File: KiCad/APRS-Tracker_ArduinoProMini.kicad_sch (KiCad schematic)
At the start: 21 parts, among them J1 Conn_01x03_Male, J2 Conn_01x05_Male, Q1 BS170, Q2 MCP1700-3302E_TO92, SW1 SW_Push, SW2 SW_SPDT, U1 Arduino-Pro-Mini, U2 TP4056

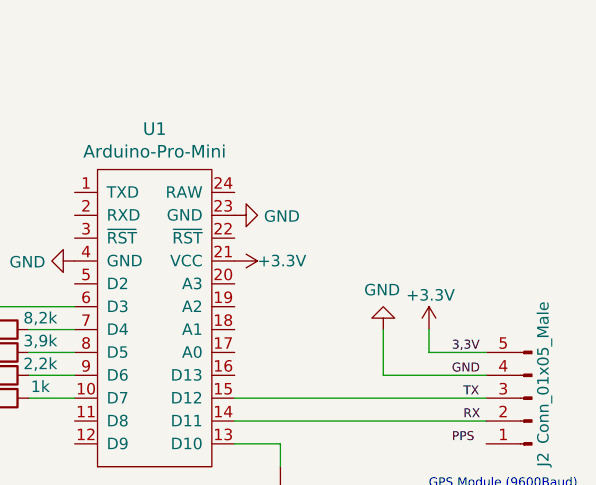
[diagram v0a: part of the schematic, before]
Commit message: Added fix LED
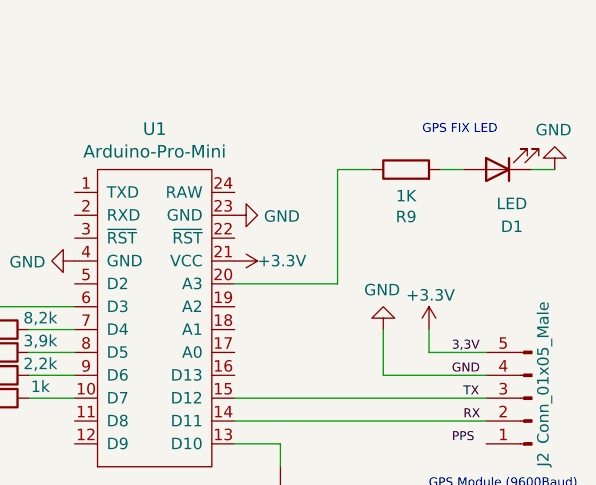
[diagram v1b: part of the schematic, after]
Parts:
- added D1: LED, LED_THT:LED_D3.0mm, symbol Device:LED
- added R9: 1K, Resistor_THT:R_Axial_DIN0204_L3.6mm_D1.6mm_P7.62mm_Horizontal, symbol Device:R
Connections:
- net GND: now also D1.1 (K)
- net at U1.20 (A3): now also R9.1
- new net: D1.2 (A), R9.2
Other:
- note added: "GPS FIX LED"
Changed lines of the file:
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@@
+    (stroke (width 0) (type default))
+  )
+  (wire (pts (xy 168.91 95.25) (xy 166.37 95.25))
     (stroke (width 0) (type default))
   )
@@
     (stroke (width 0) (type default))
   )
+  (wire (pts (xy 154.94 107.95) (xy 154.94 95.25))
+    (stroke (width 0) (type default))
+  )
   (wire (pts (xy 113.03 115.57) (xy 106.68 115.57))
     (stroke (width 0) (type default))
@@
     (stroke (width 0) (type default))
   )
+  (wire (pts (xy 179.07 95.25) (xy 176.53 95.25))
+    (stroke (width 0) (type default))
+  )
   (wire (pts (xy 146.05 177.8) (xy 146.05 180.34))
     (stroke (width 0) (type default))
@@
     (stroke (width 0) (type default))
   )
+  (wire (pts (xy 154.94 95.25) (xy 158.75 95.25))
+    (stroke (width 0) (type default))
+  )
   (wire (pts (xy 85.09 176.53) (xy 85.09 177.8))
     (stroke (width 0) (type default))
@@
   )
   (wire (pts (xy 160.02 118.11) (xy 171.45 118.11))
+    (stroke (width 0) (type default))
+  )
+  (wire (pts (xy 143.51 107.95) (xy 154.94 107.95))
     (stroke (width 0) (type default))
   )
@@
     (at 29.21 86.36 0)
     (effects (font (size 1.1938 1.1938) italic) (justify left bottom))
+  )
+  (text "GPS FIX LED" (at 172.72 91.44 0)
+    (effects (font (size 0.9906 0.9906)) (justify right bottom))
   )
   (label "GND" (at 167.64 118.11 0) (fields_autoplaced)
@@
         )
       )
+    )
+  )
+  (symbol (lib_id "Device:R") (at 162.56 95.25 90) (unit 1)
+    (in_bom yes) (on_board yes) (dnp no)
+    (property "Reference" "R9" (at 162.56 100.5078 90)
+      (effects (font (size 1.27 1.27)))
+    )
+    (property "Value" "1K" (at 162.56 98.1964 90)
+      (effects (font (size 1.27 1.27)))
+    )
+    (property "Footprint" "Resistor_THT:R_Axial_DIN0204_L3.6mm_D1.6mm_P7.62mm_Horizontal" (at 162.56 97.028 90)
+      (effects (font (size 1.27 1.27)) hide)
+    )
+    (property "Datasheet" "~" (at 162.56 95.25 0)
+      (effects (font (size 1.27 1.27)) hide)
+    )
+    (pin "1")
+    (pin "2")
+    (instances
+      (project "APRS-Tracker_ArduinoProMini"
+        (path "/c4c7785b-cfc5-4d17-87ec-66fdf5181d79"
+          (reference "R9") (unit 1)
+        )
+      )
+    )
+  )
+  (symbol (lib_id "Device:LED") (at 172.72 95.25 180) (unit 1)
+    (in_bom yes) (on_board yes) (dnp no) (fields_autoplaced)
+    (property "Reference" "D1" (at 174.3075 101.6 0)
+      (effects (font (size 1.27 1.27)))
+    )
+    (property "Value" "LED" (at 174.3075 99.06 0)
+      (effects (font (size 1.27 1.27)))
+    )
+    (property "Footprint" "LED_THT:LED_D3.0mm" (at 172.72 95.25 0)
+      (effects (font (size 1.27 1.27)) hide)
+    )
+    (property "Datasheet" "~" (at 172.72 95.25 0)
+      (effects (font (size 1.27 1.27)) hide)
+    )
+    (pin "2")
+    (pin "1")
+    (instances
+      (project "APRS-Tracker_ArduinoProMini"
+        (path "/c4c7785b-cfc5-4d17-87ec-66fdf5181d79"
+          (reference "D1") (unit 1)
+        )
+      )
+    )
+  )
+  (symbol (lib_id "power:GND") (at 179.07 95.25 180) (unit 1)
+    (in_bom yes) (on_board yes) (dnp no)
+    (property "Reference" "#PWR011" (at 179.07 88.9 0)
+      (effects (font (size 1.27 1.27)) hide)
+    )
+    (property "Value" "GND" (at 178.943 90.8558 0)
+      (effects (font (size 1.27 1.27)))
+    )
+    (property "Footprint" "" (at 179.07 95.25 0)
+      (effects (font (size 1.27 1.27)) hide)
+    )
+    (property "Datasheet" "" (at 179.07 95.25 0)
+      (effects (font (size 1.27 1.27)) hide)
+    )
+    (pin "1")
+    (instances
+      (project "APRS-Tracker_ArduinoProMini"
+        (path "/c4c7785b-cfc5-4d17-87ec-66fdf5181d79"
+          (reference "#PWR011") (unit 1)
+        )
+      )
